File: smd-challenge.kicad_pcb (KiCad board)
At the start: 2 copper layers, 55.4 x 38.4 mm, 20 parts, among them J1 DX07S016JA1R1500, U1 ATmega16U2-M, Y1 J49SMH-A-G-G-K-16M0

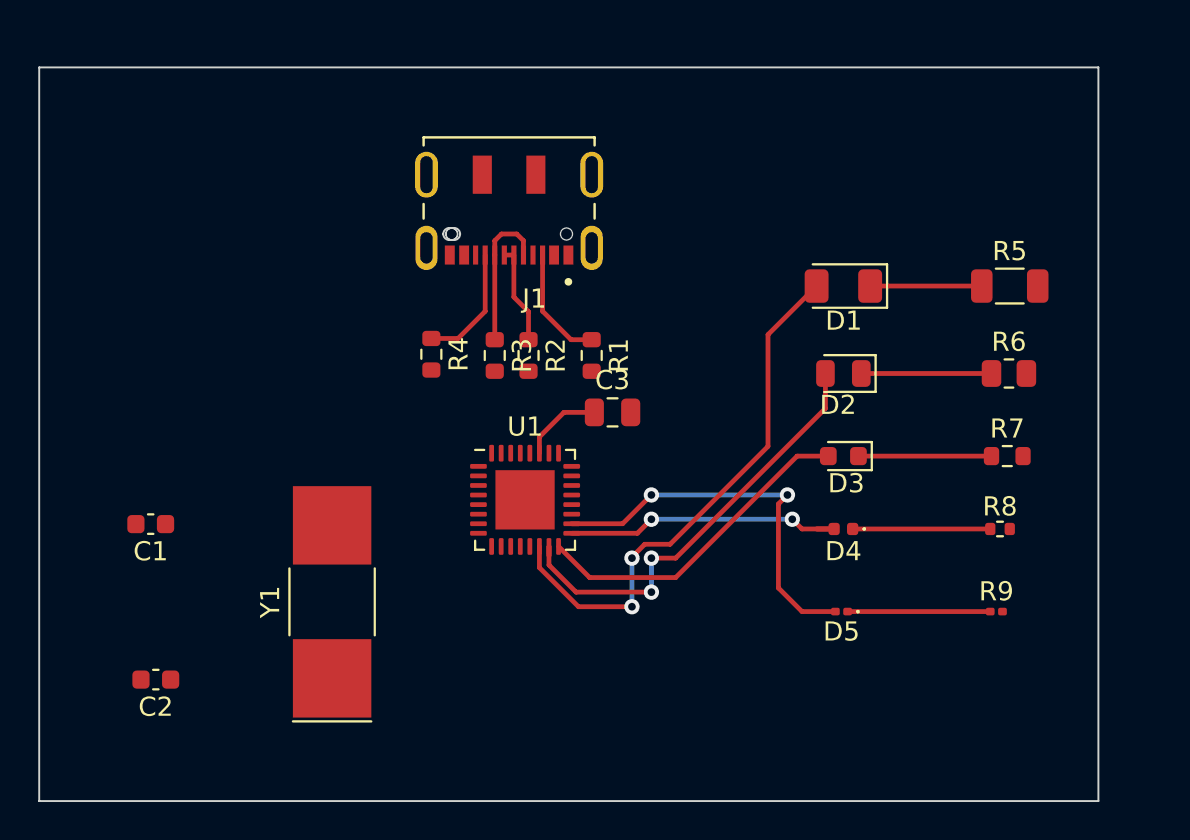
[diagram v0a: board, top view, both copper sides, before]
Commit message: Swap crystal for something smaller; settle on layout
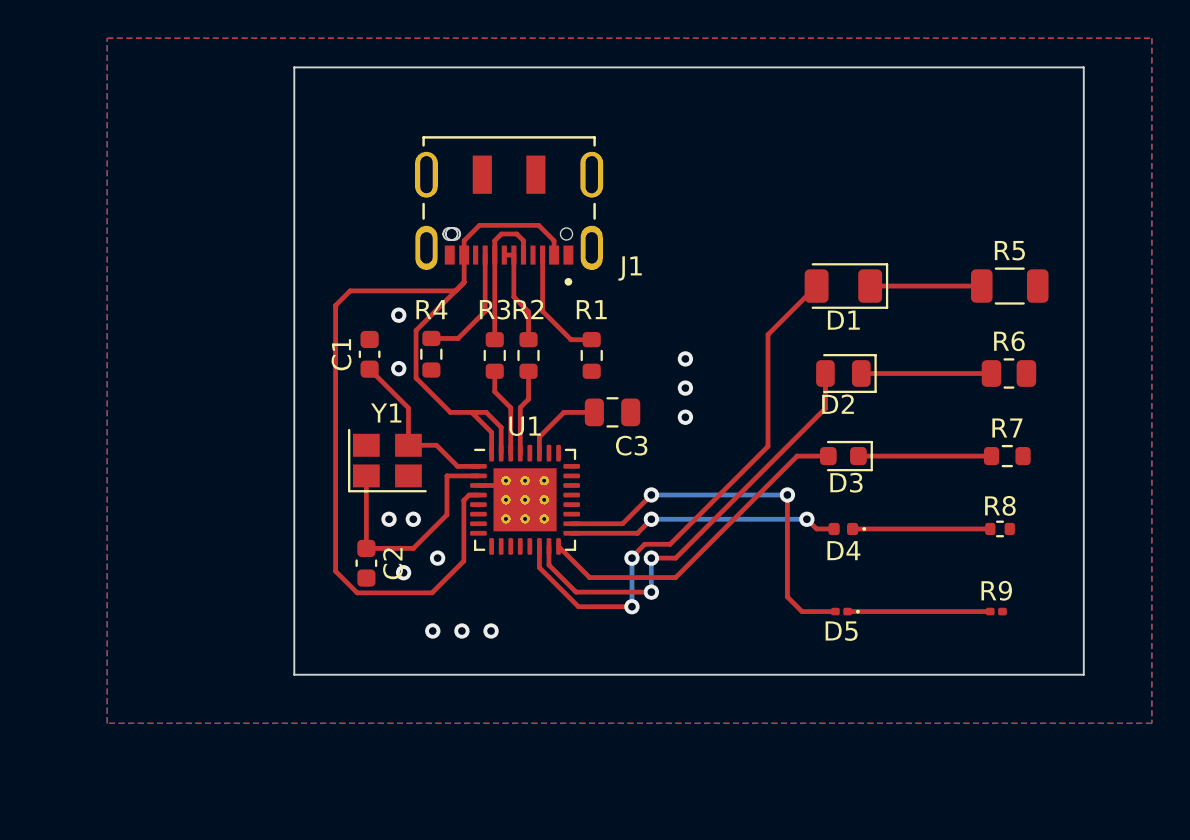
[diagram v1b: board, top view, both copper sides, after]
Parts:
- U1: footprint Package_DFN_QFN:QFN-32-1EP_5x5mm_P0.5mm_EP3.1x3.1mm -> Package_DFN_QFN:QFN-32-1EP_5x5mm_P0.5mm_EP3.3x3.3mm_ThermalVias
- Y1: value J49SMH-A-G-G-K-16M0 -> FA-238 16.0000MB-K3; footprint Crystal:Crystal_SMD_SeikoEpson_MC405-2Pin_9.6x4.1mm -> Crystal:Crystal_SMD_SeikoEpson_FA238-4Pin_3.2x2.5mm
- moved C1 14.5 mm to (124.0, 52.8), turned to 90 degrees
- moved C2 12.6 mm to (123.8, 63.8), turned to -90 degrees
- moved Y1 7.93 mm to (124.9, 58.4), turned to 0 degrees
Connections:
- Y1 pad 2: Net-(C1-Pad1) -> GND
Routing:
- net +5V: track 0.00 -> 56.8 mm
- net Net-(C2-Pad1): track 0.00 -> 12.4 mm
- net Net-(C1-Pad1): track 0.00 -> 8.94 mm
- net Net-(R3-Pad2): track 0.00 -> 4.63 mm
- net Net-(R2-Pad2): track 0.00 -> 4.46 mm
- net GND: track 0.00 -> 3.10 mm, vias 0 -> 12
- net Net-(D4-Pad2): track 15.1 -> 14.2 mm
- added copper zone on B.Cu, net GND
- added copper zone on F.Cu, net GND
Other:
- board size 55.4 x 38.4 mm -> 41.3 x 31.8 mm

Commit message: Layout with the SAMD21.
The only thing I really don't like is the snakey 3.3V rail but since I
can stitch the grounds back together via the B.Cu zone, it's mostly
fine.
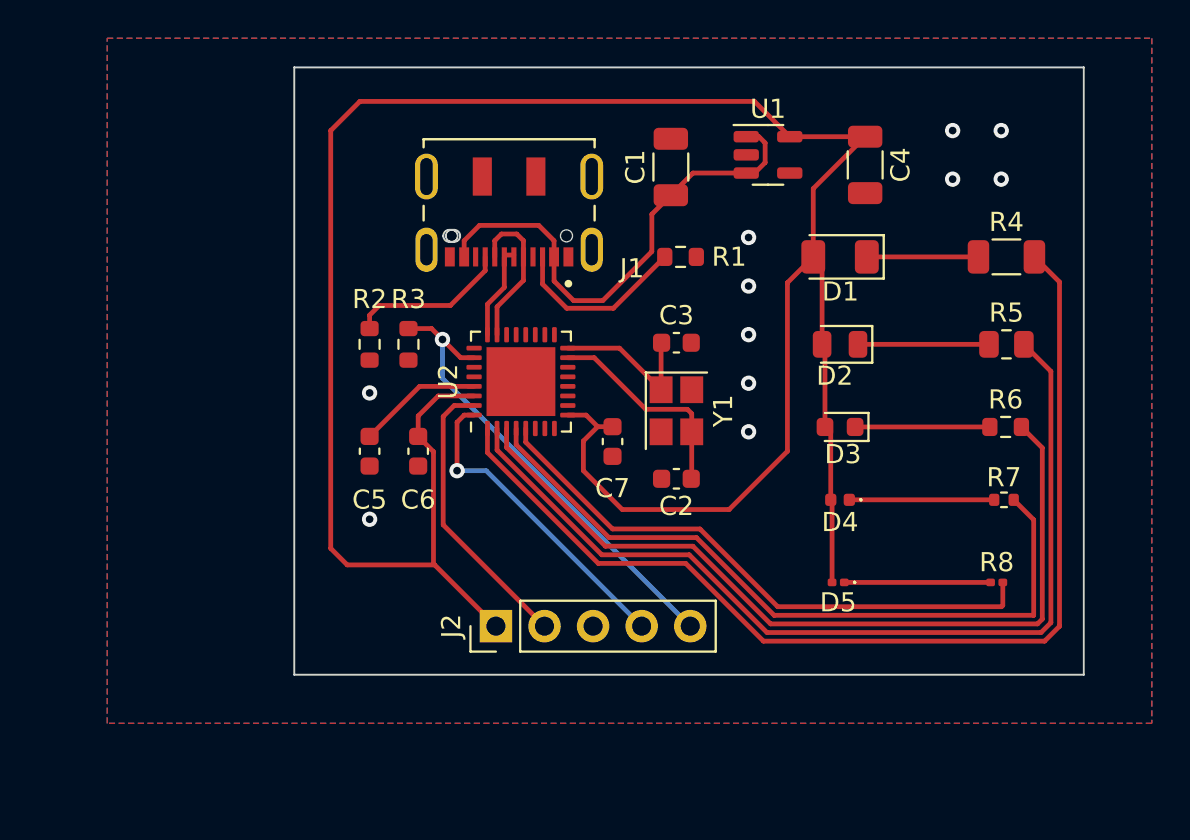
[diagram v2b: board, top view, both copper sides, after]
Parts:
- removed R9: R, Resistor_SMD:R_0201_0603Metric
- added C4: 10u, Capacitor_SMD:C_1206_3216Metric, F.Cu at (149.9, 42.9)
- added C5: 100n, Capacitor_SMD:C_0603_1608Metric, F.Cu at (124.0, 57.9)
- added C6: 100n, Capacitor_SMD:C_0603_1608Metric, F.Cu at (126.5, 57.9)
- added C7: 100n, Capacitor_SMD:C_0603_1608Metric, F.Cu at (136.7, 57.4)
- added J2: Conn_01x05, Connector_PinHeader_2.54mm:PinHeader_1x05_P2.54mm_Vertical, F.Cu at (130.6, 67.1)
- added U2: ATSAMD21E15B-M, Package_DFN_QFN:QFN-32-1EP_5x5mm_P0.5mm_EP3.6x3.6mm, F.Cu at (131.9, 54.3)
- C1: value 16p -> 10u; footprint Capacitor_SMD:C_0603_1608Metric -> Capacitor_SMD:C_1206_3216Metric
- C2: value 16p -> 12p
- C3: value 1u -> 12p; footprint Capacitor_SMD:C_0805_2012Metric -> Capacitor_SMD:C_0603_1608Metric
- R2: value 39R -> 5k1
- R3: value 39R -> 10k
- R4: value 5k1 -> R; footprint Resistor_SMD:R_0603_1608Metric -> Resistor_SMD:R_1206_3216Metric
- R5: footprint Resistor_SMD:R_1206_3216Metric -> Resistor_SMD:R_0805_2012Metric
- R6: footprint Resistor_SMD:R_0805_2012Metric -> Resistor_SMD:R_0603_1608Metric
- R7: footprint Resistor_SMD:R_0603_1608Metric -> Resistor_SMD:R_0402_1005Metric
- R8: footprint Resistor_SMD:R_0402_1005Metric -> Resistor_SMD:R_0201_0603Metric
- U1: value ATmega16U2-M -> MIC5504-3.3YM5; footprint Package_DFN_QFN:QFN-32-1EP_5x5mm_P0.5mm_EP3.3x3.3mm_ThermalVias -> Package_TO_SOT_SMD:SOT-23-5
- moved R4 30.5 mm to (157.2, 47.8), turned to 0 degrees
- moved U1 22.1 mm to (144.8, 42.4)
- moved C1 18.5 mm to (139.7, 43.1)
- moved C2 16.8 mm to (140.0, 59.4), turned to 180 degrees
- moved Y1 15.3 mm to (140.0, 55.8), turned to -90 degrees
- moved R2 8.33 mm to (124.0, 52.3)
- moved R1 6.94 mm to (140.2, 47.8), turned to 0 degrees
- moved C3 4.94 mm to (140.0, 52.2)
- moved R3 4.55 mm to (126.0, 52.3)
- moved R5 3.05 mm to (157.2, 52.3)
- moved R6 2.80 mm to (157.2, 56.6)
- moved R8 2.80 mm to (156.7, 64.8)
- moved R7 2.29 mm to (157.1, 60.5)
- moved D1 1.53 mm to (148.5, 47.8)
- moved D2 1.53 mm to (148.5, 52.3)
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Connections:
- C1 pad 1: Net-(C1-Pad1) -> +5V
- D1 pad 2: Net-(D1-Pad2) -> +3V3
- D2 pad 2: Net-(D2-Pad2) -> +3V3
- D3 pad 2: Net-(D3-Pad2) -> +3V3
- D4 pad 2: Net-(D4-Pad2) -> +3V3
- D5 pad 2: Net-(D5-Pad2) -> +3V3
- R2 pad 1: Net-(J1-Pad6) -> Net-(J1-Pad9)
- R2 pad 2: Net-(R2-Pad2) -> GND
- R3 pad 1: Net-(J1-Pad5) -> /NRST
- R3 pad 2: Net-(R3-Pad2) -> GND
- R4 pad 1: Net-(J1-Pad9) -> Net-(D1-Pad1)
- R4 pad 2: GND -> /RED
- R5 pad 1: Net-(D1-Pad1) -> Net-(D2-Pad1)
- R5 pad 2: GND -> /ORANGE
- R6 pad 1: Net-(D2-Pad1) -> Net-(D3-Pad1)
- R6 pad 2: GND -> /YELLOW
- R7 pad 1: Net-(D3-Pad1) -> Net-(D4-Pad1)
- R7 pad 2: GND -> /GREEN
- R8 pad 1: Net-(D4-Pad1) -> Net-(D5-Pad1)
- R8 pad 2: GND -> /BLUE
- U1 pad 1: Net-(C1-Pad1) -> +5V
- U1 pad 2: Net-(C2-Pad1) -> GND
- U1 pad 3: GND -> +5V
- U1 pad 4: +5V -> unconnected-(U1-Pad4)
- U1 pad 5: unconnected-(U1-Pad5) -> +3V3
- Y1 pad 1: Net-(C2-Pad1) -> Net-(C3-Pad1)
- Y1 pad 3: Net-(C1-Pad1) -> Net-(C2-Pad1)
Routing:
- net +3V3: track 0.00 -> 125.6 mm
- net /RED: track 0.00 -> 55.4 mm
- net /ORANGE: track 0.00 -> 49.4 mm
- net /YELLOW: track 0.00 -> 43.4 mm
- net /GREEN: track 0.00 -> 38.1 mm
- net +5V: track 56.8 -> 25.4 mm
- net /BLUE: track 0.00 -> 30.5 mm
- net Net-(D1-Pad2): track 28.3 -> 0.00 mm, vias 2 -> 0
- net /NRST: track 0.00 -> 24.4 mm, vias 0 -> 1
- net Net-(D2-Pad2): track 22.9 -> 0.00 mm, vias 2 -> 0
- net Net-(D5-Pad2): track 20.1 -> 0.00 mm, vias 2 -> 0
- net Net-(D3-Pad2): track 17.4 -> 0.00 mm
- net /SWDIO: track 0.00 -> 16.6 mm, vias 0 -> 1
- net /SWCLK: track 0.00 -> 15.0 mm
- net Net-(D4-Pad2): track 14.2 -> 0.00 mm, vias 2 -> 0
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
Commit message: PCB: swap through-hole for SMD header
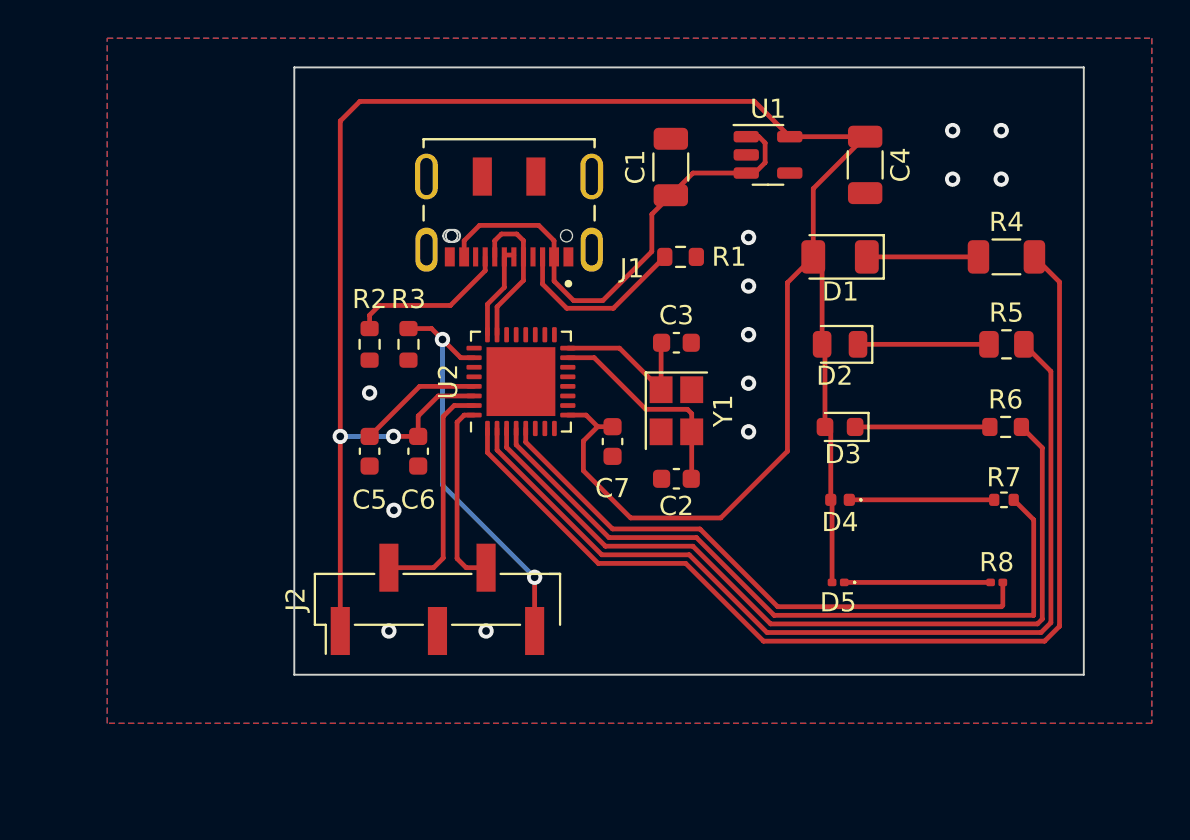
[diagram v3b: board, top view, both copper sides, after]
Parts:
- J2: footprint Connector_PinHeader_2.54mm:PinHeader_1x05_P2.54mm_Vertical -> Connector_PinHeader_2.54mm:PinHeader_1x05_P2.54mm_Vertical_SMD_Pin1Left
- R4, R6: value R -> 260
- R5: value R -> 240
- R7: value R -> 130
- R8: value R -> 80
- moved J2 3.36 mm to (127.5, 65.7)
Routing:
- net +3V3: track 125.6 -> 116.8 mm, vias 0 -> 2
- net /SWDIO: track 16.6 -> 9.89 mm, vias 1 -> 0
- net /NRST: track 24.4 -> 21.3 mm, vias 1 -> 2
- net /SWCLK: track 15.0 -> 12.3 mm
- net GND: vias 11 -> 13
